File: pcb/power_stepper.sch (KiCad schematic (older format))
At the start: 49 parts, among them J2 1757284, U16 UCC12040, U17 ISO7762, U2 powerSTEP01

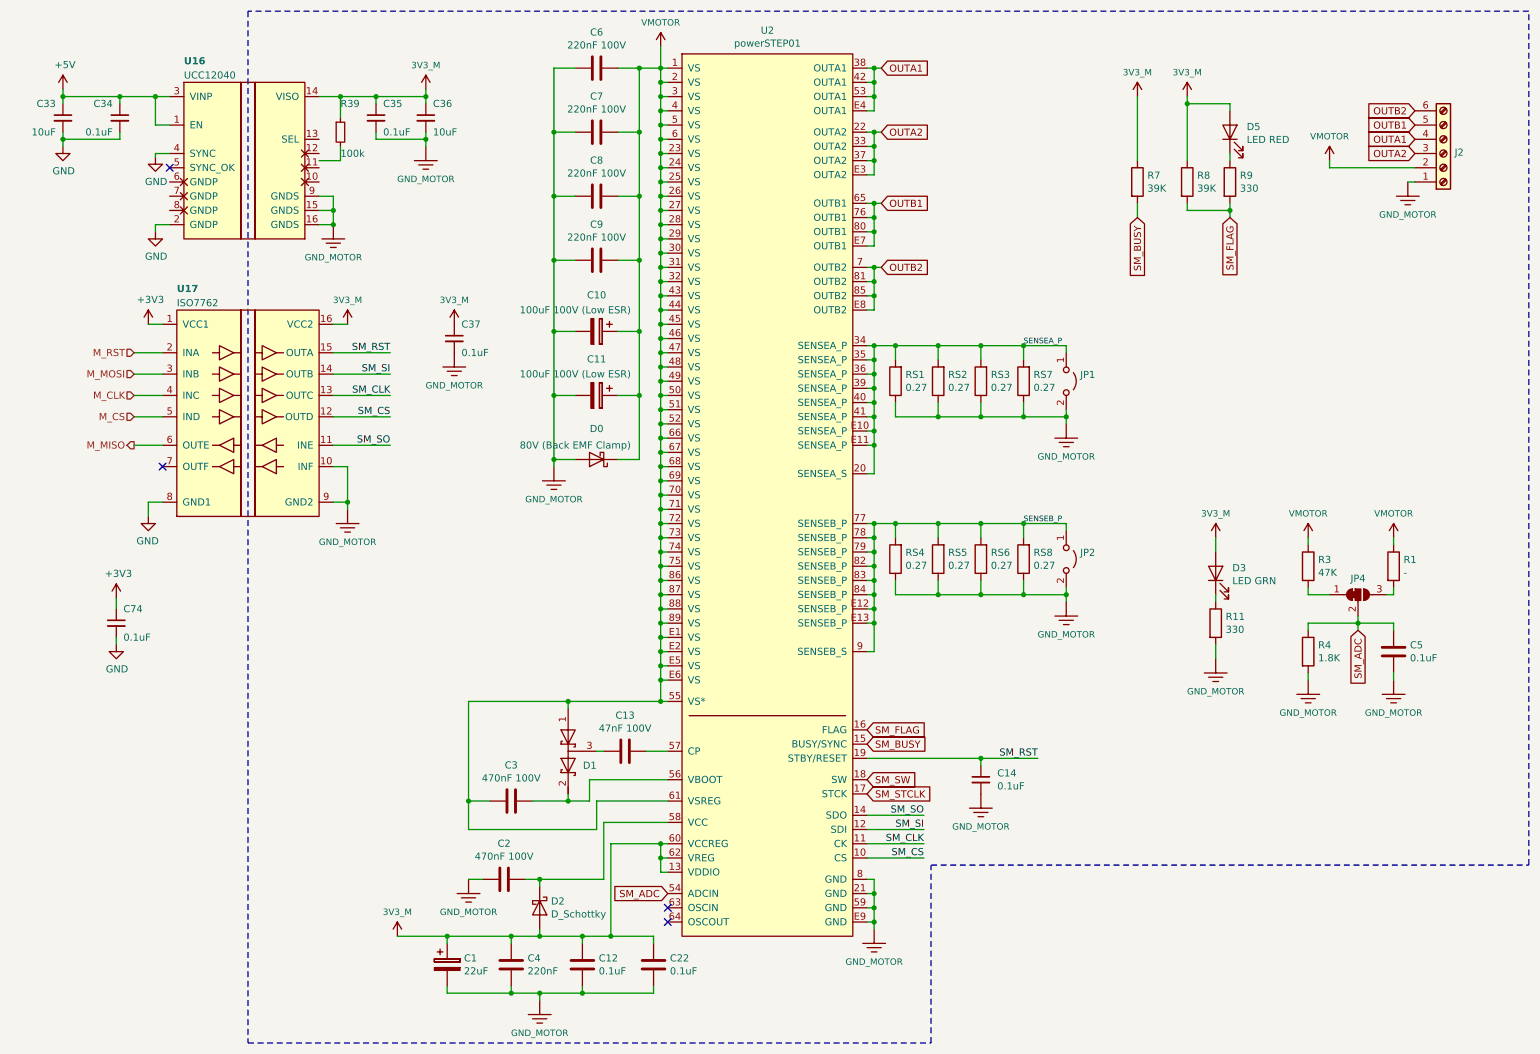
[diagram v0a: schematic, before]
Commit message: Solved connection problem with XCL214B333DR and it was added 3 leds to the board
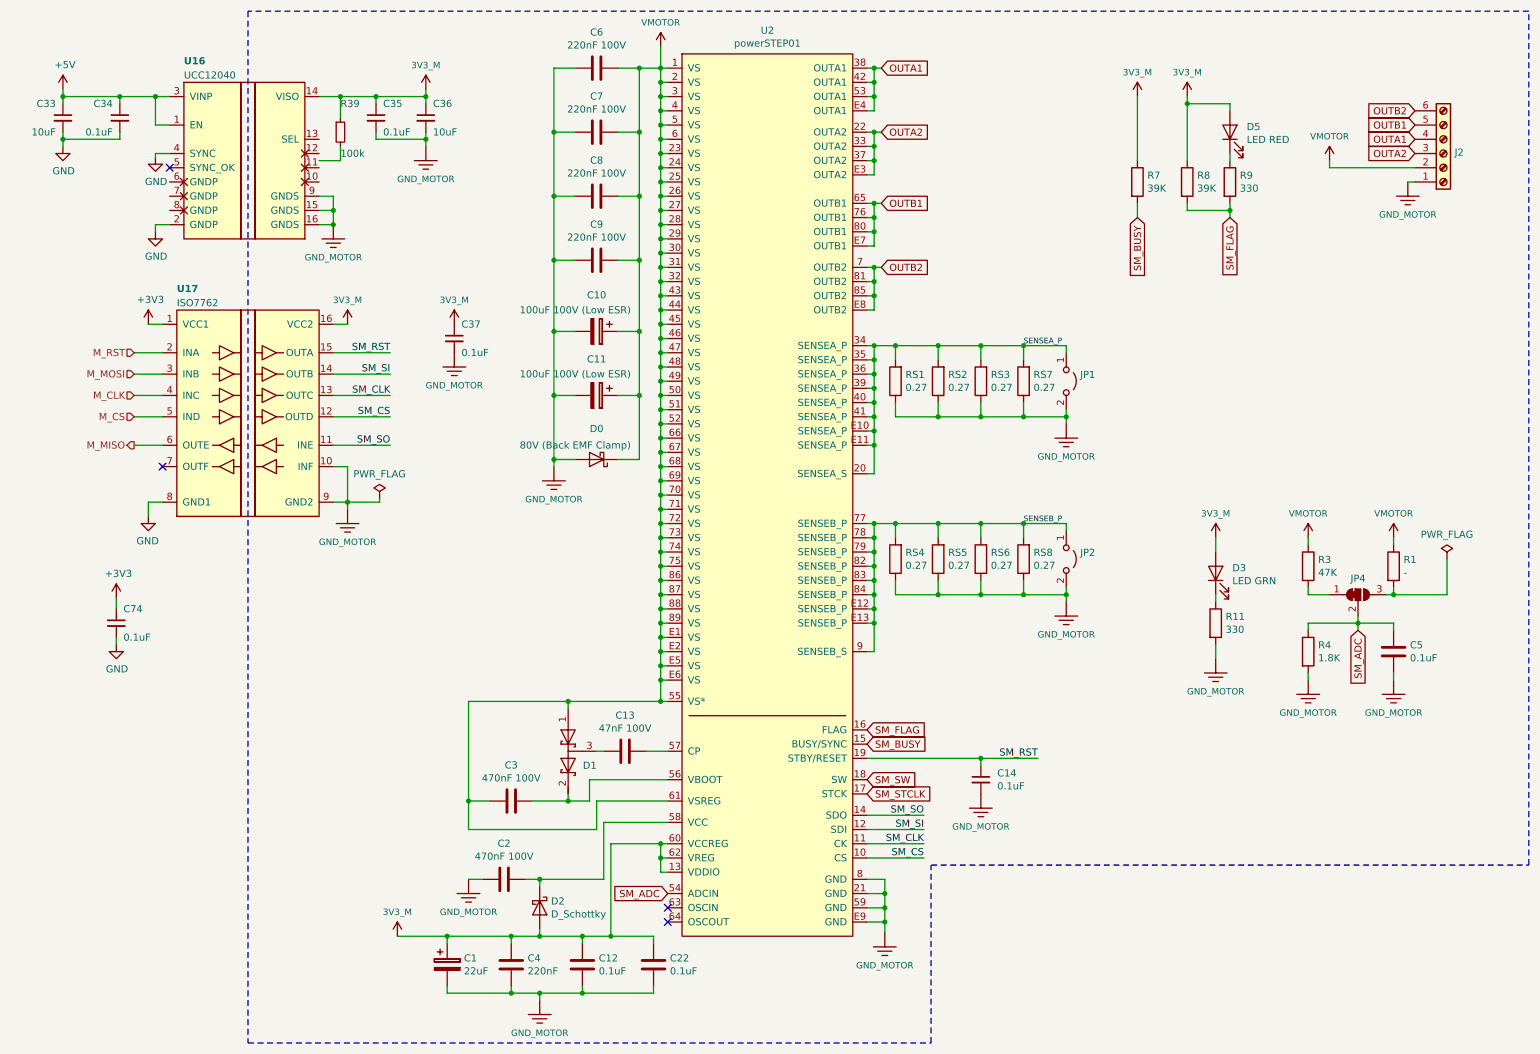
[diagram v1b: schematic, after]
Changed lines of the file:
@@
 Connection ~ 4250 3200
 NoConn ~ 5050 6900
-Wire Wire Line
-	6500 6950 6500 6900
-Wire Wire Line
-	6500 6600 6450 6600
-Wire Wire Line
-	6450 6700 6500 6700
-Connection ~ 6500 6700
-Wire Wire Line
-	6500 6700 6500 6600
-Wire Wire Line
-	6500 6800 6450 6800
-Connection ~ 6500 6800
-Wire Wire Line
-	6500 6800 6500 6700
-Wire Wire Line
-	6450 6900 6500 6900
-Connection ~ 6500 6900
-Wire Wire Line
-	6500 6900 6500 6800
 $Comp
 L Device:C C3
@@
 L ventilator-PowerSymbols:GND_MOTOR #GND0115
 U 1 1 5EBD4224
-P 6500 6950
-F 0 "#GND0115" H 6550 6900 45  0001 L BNN
-F 1 "GND_MOTOR" H 6500 6720 45  0000 C CNN
-F 2 "" H 6500 6950 50  0001 C CNN
-F 3 "" H 6500 6850 60  0001 C CNN
-	1    6500 6950
+P 6575 6975
+F 0 "#GND0115" H 6625 6925 45  0001 L BNN
+F 1 "GND_MOTOR" H 6575 6745 45  0000 C CNN
+F 2 "" H 6575 6975 50  0001 C CNN
+F 3 "" H 6575 6875 60  0001 C CNN
+	1    6575 6975
 	1    0    0    -1
 $EndComp
@@
 Wire Wire Line
 	1175 4900 1175 4950
+Wire Wire Line
+	6575 6975 6575 6900
+Wire Wire Line
+	6575 6600 6450 6600
+Wire Wire Line
+	6450 6700 6575 6700
+Connection ~ 6575 6700
+Wire Wire Line
+	6575 6700 6575 6600
+Wire Wire Line
+	6450 6800 6575 6800
+Connection ~ 6575 6800
+Wire Wire Line
+	6575 6800 6575 6700
+Wire Wire Line
+	6450 6900 6575 6900
+Connection ~ 6575 6900
+Wire Wire Line
+	6575 6900 6575 6800
+$Comp
+L power:PWR_FLAG #FLG0101
+U 1 1 5F1397A3
+P 3025 3925
+F 0 "#FLG0101" H 3025 4000 50  0001 C CNN
+F 1 "PWR_FLAG" H 3025 4098 50  0000 C CNN
+F 2 "" H 3025 3925 50  0001 C CNN
+F 3 "~" H 3025 3925 50  0001 C CNN
+	1    3025 3925
+	1    0    0    -1
+$EndComp
+Wire Wire Line
+	3025 3925 3025 3950
+Wire Wire Line
+	3025 3950 2800 3950
+$Comp
+L power:PWR_FLAG #FLG0102
+U 1 1 5F164ACB
+P 10525 4350
+F 0 "#FLG0102" H 10525 4425 50  0001 C CNN
+F 1 "PWR_FLAG" H 10525 4523 50  0000 C CNN
+F 2 "" H 10525 4350 50  0001 C CNN
+F 3 "~" H 10525 4350 50  0001 C CNN
+	1    10525 4350
+	1    0    0    -1
+$EndComp
+Wire Wire Line
+	10525 4600 10150 4600
+Wire Wire Line
+	10525 4350 10525 4600
+Connection ~ 10150 4600
 $EndSCHEMATC

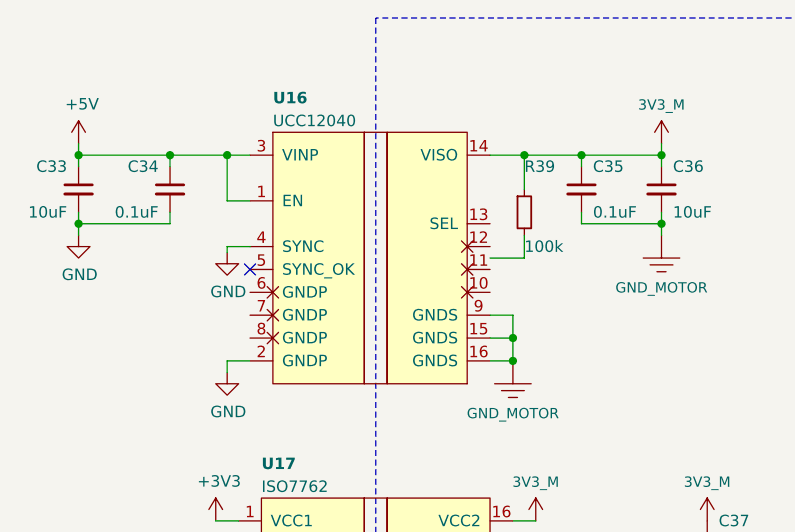
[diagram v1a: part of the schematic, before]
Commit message: Solved all troubles with Torex footprints and copper zones
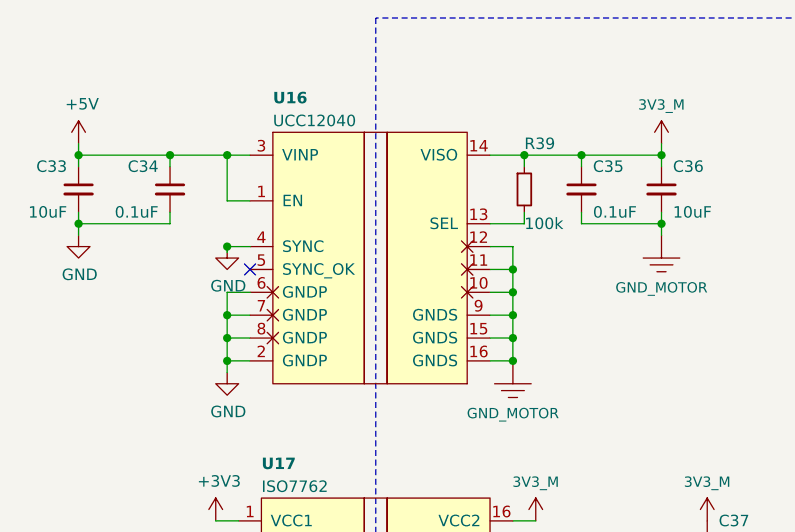
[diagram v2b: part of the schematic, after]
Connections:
- net GND: now also U16.6 (GNDP), U16.7 (GNDP), U16.8 (GNDP)
- net GND_MOTOR: now also U16.10, U16.11, U16.12
- net at R39.2: now also U16.13 (SEL)
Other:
- moved on the sheet: R39
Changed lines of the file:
@@
 L Device:R_Small R39
 U 1 1 5E97E61C
-P 2750 1350
-F 0 "R39" H 2750 1550 50  0000 L CNN
-F 1 "100k" H 2750 1200 50  0000 L CNN
-F 2 "Resistor_SMD:R_0402_1005Metric" H 2750 1350 50  0001 C CNN
-F 3 "~" H 2750 1350 50  0001 C CNN
-	1    2750 1350
+P 2750 1250
+F 0 "R39" H 2750 1450 50  0000 L CNN
+F 1 "100k" H 2750 1100 50  0000 L CNN
+F 2 "Resistor_SMD:R_0402_1005Metric" H 2750 1250 50  0001 C CNN
+F 3 "~" H 2750 1250 50  0001 C CNN
+	1    2750 1250
 	1    0    0    -1
 $EndComp
@@
 Connection ~ 3350 1400
 Wire Wire Line
-	2750 1250 2750 1100
+	2750 1150 2750 1100
 Connection ~ 2750 1100
 Wire Wire Line
 	2750 1100 3000 1100
-Wire Wire Line
-	2750 1450 2750 1550
-Wire Wire Line
-	2750 1550 2600 1550
 $Comp
 L power:GND #PWR0114
@@
 L power:GND #PWR0142
 U 1 1 5EB83B21
-P 1450 1525
-F 0 "#PWR0142" H 1450 1275 50  0001 C CNN
-F 1 "GND" H 1455 1352 50  0000 C CNN
-F 2 "" H 1450 1525 50  0001 C CNN
-F 3 "" H 1450 1525 50  0001 C CNN
-	1    1450 1525
+P 1450 1500
+F 0 "#PWR0142" H 1450 1250 50  0001 C CNN
+F 1 "GND" H 1455 1327 50  0000 C CNN
+F 2 "" H 1450 1500 50  0001 C CNN
+F 3 "" H 1450 1500 50  0001 C CNN
+	1    1450 1500
 	1    0    0    -1
 $EndComp
@@
 	10525 4350 10525 4600
 Connection ~ 10150 4600
+Connection ~ 1450 1500
+Wire Wire Line
+	1550 1900 1450 1900
+Wire Wire Line
+	1450 1900 1450 2000
+Connection ~ 1450 2000
+Wire Wire Line
+	1550 1800 1450 1800
+Wire Wire Line
+	1450 1800 1450 1900
+Connection ~ 1450 1900
+Wire Wire Line
+	1550 1700 1450 1700
+Wire Wire Line
+	1450 1700 1450 1800
+Connection ~ 1450 1800
+Wire Wire Line
+	2600 1400 2750 1400
+Wire Wire Line
+	2750 1400 2750 1350
+Wire Wire Line
+	2600 1500 2700 1500
+Wire Wire Line
+	2700 1500 2700 1600
+Connection ~ 2700 1800
+Wire Wire Line
+	2600 1700 2700 1700
+Connection ~ 2700 1700
+Wire Wire Line
+	2700 1700 2700 1800
+Wire Wire Line
+	2600 1600 2700 1600
+Connection ~ 2700 1600
+Wire Wire Line
+	2700 1600 2700 1700
 $EndSCHEMATC

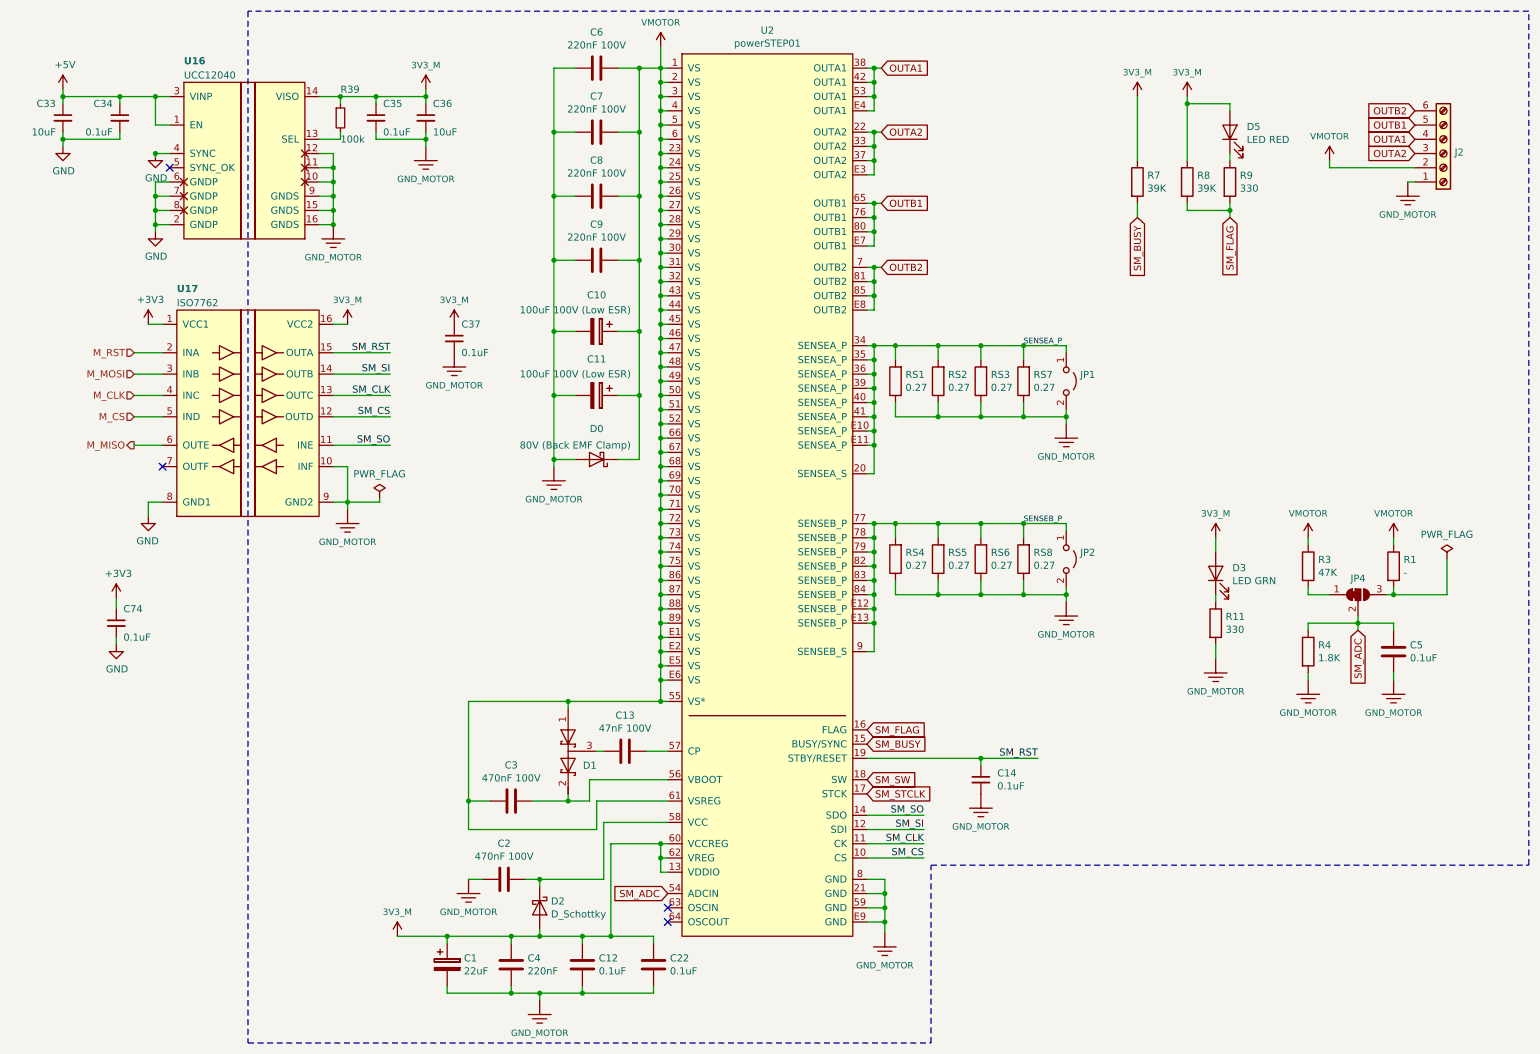
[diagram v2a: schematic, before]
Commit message: Added 3d shape for connector clik-mate Added connection between STM and connector clik-mate on schema and PCB P3 is a connector that allows put a panic button for do a reset in the IC powerstep01
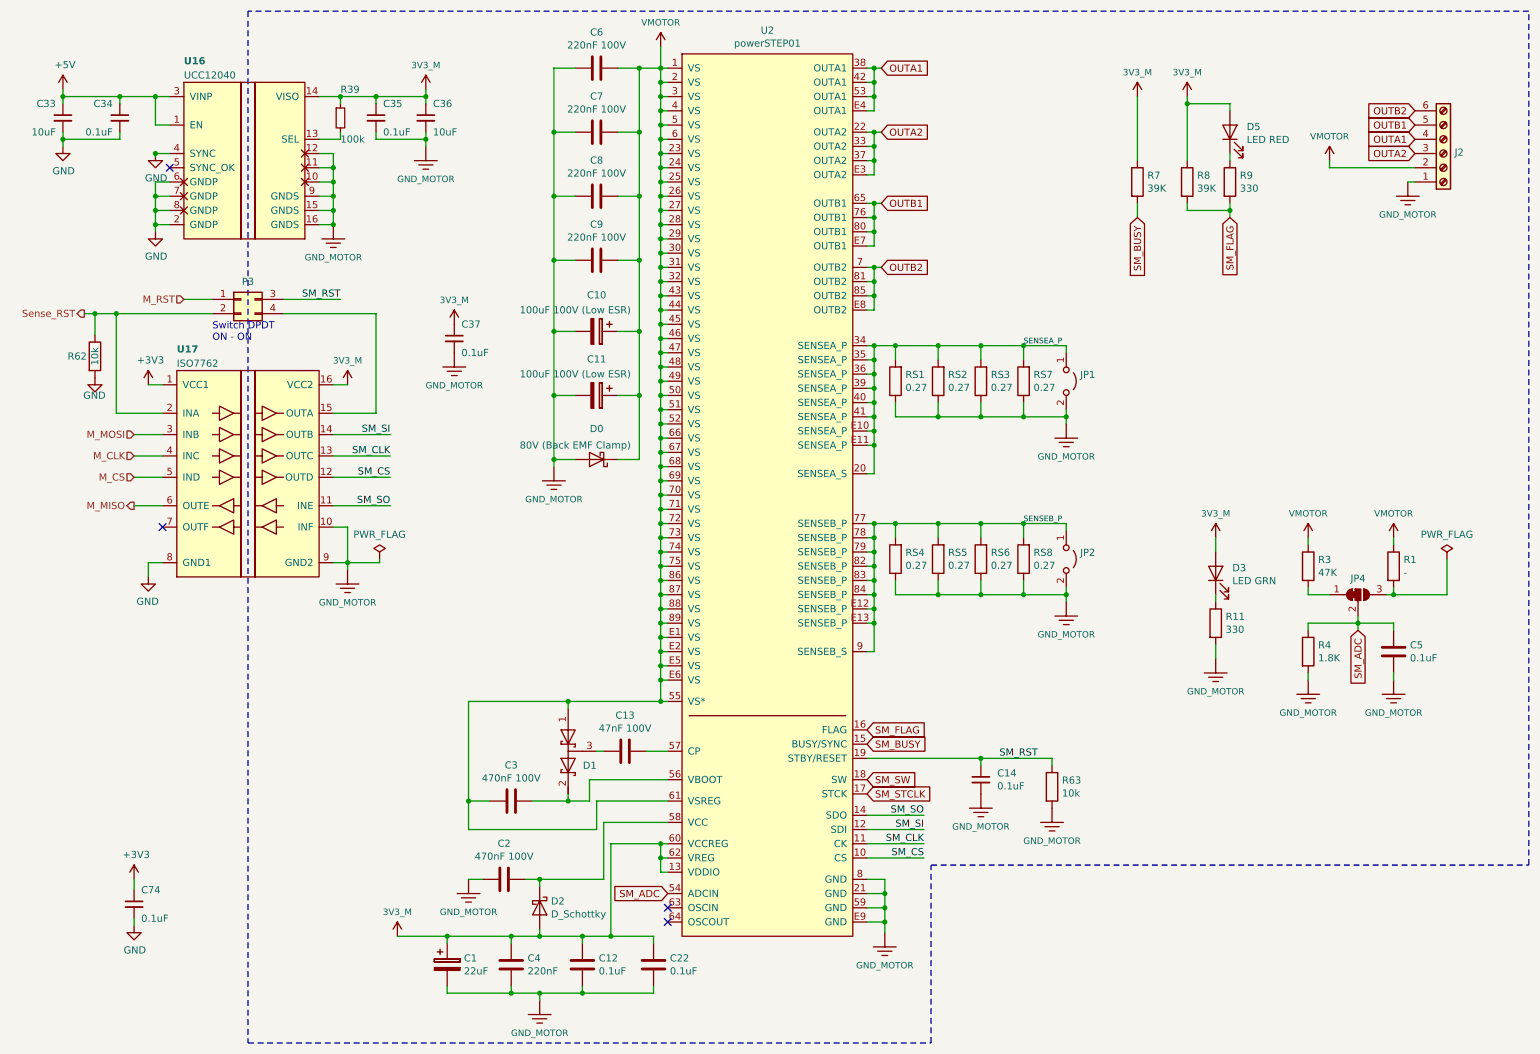
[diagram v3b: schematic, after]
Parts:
- added P3: CONN_02X02, Connector_Molex:Molex_CLIK-Mate_502443-0470_1x04-1MP_P2.00mm_Vertical, symbol Connector_Generic:Conn_02x02_Top_Bottom
- added R62, R63: 10k, Resistor_SMD:R_0402_1005Metric, symbol Device:R
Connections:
- net GND: now also R62.2
- net GND_MOTOR: now also R63.2
- net M_RST: now also P3.1 (Pin_1); no longer U17.2 (INA)
- net SM_RST: now also P3.3 (Pin_3), R63.1; no longer U17.15 (OUTA)
- new net: P3.4 (Pin_4), U17.15 (OUTA)
- new net Sense_RST: P3.2 (Pin_2), R62.1, U17.2 (INA)
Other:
- note added: "Switch DPDT\nON - ON"
- moved on the sheet: C74, U17
